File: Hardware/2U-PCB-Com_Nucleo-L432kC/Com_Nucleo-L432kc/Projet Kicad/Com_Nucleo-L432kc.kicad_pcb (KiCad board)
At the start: 2 copper layers, 90 x 92 mm, 46 parts, among them IC1 PCI_EXPRESS_CARD, J1 Bus Standard, J2 I2C_Grove, J3 I2C_Grove, J4 Conn_01x08, J5 Conn_01x08, J6 Conn_01x15, J7 Conn_01x15, J8 I2C_Grove, J9 I2C_Grove, SW101 Jumper_RESET_L432KC_Open, SW102 Jumper_MCU_Reset_Open, SW103 Jumper_SX1303_Reset_Open, U1 7404

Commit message: routage terminé
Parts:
- removed B1, B2: SN74AHC1G125DBVT, Package_SO:TSOP-5_1.65x3.05mm_P0.95mm
- removed C11: 100n, Capacitor_SMD:C_0805_2012Metric_Pad1.18x1.45mm_HandSolder
- removed the C7 at (135.9, 60.6)
- removed the C8 at (132.9, 60.6)
- removed the J2 at (79.0, 51.0)
- removed the J4 at (70.9, 79.6)
- removed R4, R5: 100, Resistor_SMD:R_0805_2012Metric_Pad1.20x1.40mm_HandSolder
- removed REF** (x2): MountingHole_2.7mm_M2.5_Pad, MountingHole:MountingHole_2.7mm_M2.5_Pad
- removed SW102: Jumper_MCU_Reset_Open, Button_Switch_THT:SW_PUSH_6mm
- removed SW103: Jumper_SX1303_Reset_Open, Button_Switch_THT:SW_PUSH_6mm
- removed U1: 7404, Library:N14
- added JP1: PWM1_SEL, Connector_PinHeader_1.27mm:PinHeader_1x03_P1.27mm_Vertical, F.Cu at (132.8, 122.8)
- added JP3: RX_SEL, Connector_PinHeader_1.27mm:PinHeader_1x03_P1.27mm_Vertical, F.Cu at (149.4, 125.4)
- added JP5: INT_SEL, Connector_PinHeader_1.27mm:PinHeader_1x03_P1.27mm_Vertical, F.Cu at (139.3, 125.4)
- added R10: 0, Resistor_SMD:R_0805_2012Metric_Pad1.20x1.40mm_HandSolder, F.Cu at (90.2, 61.9)
- added R11: 0, Resistor_SMD:R_0805_2012Metric_Pad1.20x1.40mm_HandSolder, F.Cu at (92.2, 61.8)
- added R12: 0, Resistor_SMD:R_0805_2012Metric_Pad1.20x1.40mm_HandSolder, F.Cu at (87.3, 61.8)
- added R13: 0, Resistor_SMD:R_0805_2012Metric_Pad1.20x1.40mm_HandSolder, F.Cu at (85.3, 61.8)
- added R14: 0, Resistor_SMD:R_0805_2012Metric_Pad1.20x1.40mm_HandSolder, F.Cu at (82.4, 61.8)
- added R15: 0, Resistor_SMD:R_0805_2012Metric_Pad1.20x1.40mm_HandSolder, F.Cu at (80.4, 61.8)
- added R8: 0, Resistor_SMD:R_0805_2012Metric_Pad1.20x1.40mm_HandSolder, F.Cu at (107.1, 97.8)
- added R9: 0, Resistor_SMD:R_0805_2012Metric_Pad1.20x1.40mm_HandSolder, F.Cu at (107.1, 94.6)
- added U2: MCP9808_MSOP, Package_SO:MSOP-8_3x3mm_P0.65mm, F.Cu at (77.0, 56.6)
- CR1: footprint Library:SO-8_STM -> Package_SO:SO-8_3.9x4.9mm_P1.27mm
- G*** (x2): footprint Com Nucleo library:logo_csug -> Com_L432KC_footprint:logo_csug
- J1: footprint Library:flatsat_conn -> Com_L432KC_footprint:flatsat_conn
- J5: value Conn_01x08 -> MIKROE-4247; footprint Library:MIkrobus_Connector -> Com_L432KC_footprint:MIKROE4247
- JP4: value Jumper_STANDBY_GPS_Open -> TX_SEL; footprint Connector_PinHeader_2.54mm:PinHeader_1x02_P2.54mm_Vertical -> Connector_PinHeader_1.27mm:PinHeader_1x03_P1.27mm_Vertical
- R1, R2: value 0 -> 4K7
- R3: value 100 -> 4K7
- R6: value 100 -> 0
- R7: moved to F.Cu
- SW1: renamed from SW101; value Jumper_RESET_L432KC_Open -> Reset
- moved R2 82.8 mm to (94.8, 52.2), turned to -90 degrees
- moved R1 59.6 mm to (141.3, 59.6)
- moved J6 55.8 mm to (71.1, 113.4)
- moved J4 55.8 mm to (93.9, 113.4)
- moved J9 55.8 mm to (82.1, 113.4)
- moved R3 50.3 mm to (98.5, 52.2), turned to -90 degrees
- moved R6 33.6 mm to (132.1, 88.7), turned to 180 degrees
- moved R7 32.6 mm to (132.6, 63.3), turned to 180 degrees
- moved JP2 24.8 mm to (118.8, 77.9), turned to 180 degrees
- moved G*** 21.7 mm to (103.6, 109.9)
- moved JP4 21.0 mm to (145.3, 125.4), turned to 180 degrees
- moved J5 8.88 mm to (93.8, 88.5), turned to 90 degrees
- moved SW1 8.65 mm to (140.3, 56.5)
- moved G*** 3.15 mm to (85.0, 54.5)
- moved C9 2.85 mm to (115.0, 93.5)
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- renumbered C6 to C10, C13 to C2, C2 to C3, C14 to C4, C3 to C5, C4 to C6, C9 to C7, C5 to C8, C10 to C9, J7 to J2, J3 to J4, J8 to J6, J6 to J7, JP5 to JP2
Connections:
- net /CAN1_RX renamed /CAN_RX
- net /CAN1_TX renamed /CAN_TX
- net /MCU_MOSI renamed /INT1
- C7 pad 1: +3V3 -> Net-(CR1-VS)
- C9 pad 1: +3V3 -> Net-(CR1-VS)
- CR1 pad 3: +3V3 -> Net-(CR1-VS)
- IC1 pad 13: Net-(IC1-REFCLK+) -> unconnected-(IC1-REFCLK+-Pad13)
- IC1 pad 19: unconnected-(IC1-RESERVED-Pad19) -> /PPS_LORA_CORE
- IC1 pad 22: /SX1303_RESET -> /RST_LORA_CORE
- IC1 pad 23: Net-(IC1-PERn0) -> unconnected-(IC1-PERn0-Pad23)
- IC1 pad 25: /STANDBY_GPS -> unconnected-(IC1-PERp0-Pad25)
- IC1 pad 30: /SCL -> unconnected-(IC1-SMB_SCL-Pad30)
- IC1 pad 31: unconnected-(IC1-PETn0-Pad31) -> /UART_TX_LORA_CORE
- IC1 pad 32: /SDA -> unconnected-(IC1-SMB_SDA-Pad32)
- IC1 pad 33: unconnected-(IC1-PETp0-Pad33) -> /UART_RX_LORA_CORE
- IC1 pad 45: Net-(IC1-RESERVED1) -> /SCLK
- IC1 pad 47: Net-(IC1-RESERVED2) -> /MISO
- IC1 pad 49: Net-(IC1-RESERVED3) -> /MOSI
- IC1 pad 51: Net-(IC1-RESERVED4) -> /CS_LORA_CORE
- IC1 pad 6: /TH1 -> /GPIO6_SX1303
- J1 pad 11: /SENS_MAG-Y -> /SENS2
- J1 pad 17: /RX_CALC -> /UART_RX_INISAT
- J1 pad 19: /TX_CALC -> /UART_TX_INISAT
- J1 pad 3: /Vin -> +5V
- J1 pad 30: /RESET_SIGNAL -> unconnected-(J1-PWM_O_1-Pad30)
- J1 pad 4: unconnected-(J1-5V-Pad4) -> +5V
- J1 pad 6: /PWM_ROUE/MAG-X -> /PWM_INISAT
- J1 pad 8: /SENS_ROUE/MAG-X -> /SENS1
- J1 pad 9: /PWM_MAG-Y -> /PWM2
- J2 pad 10: unconnected-(J7-Pin_10-Pad10) -> Net-(J2-Pin_10)
- J2 pad 11: unconnected-(J7-Pin_11-Pad11) -> Net-(J2-Pin_11)
- J2 pad 12: /PWM_ROUE/MAG-X -> /PWM1
- J2 pad 14: /MCU_NRESET -> /MOSI
- J2 pad 15: /CS_MCU -> /MISO
- J2 pad 3: /L432KC_RESET -> /RESET_GENERAL
- J2 pad 6: /PWM_MAG-Y -> /RST_LORA_CORE
- J2 pad 7: /RX_CALC -> /UART_RX_1
- J2 pad 8: /TX_CALC -> /UART_TX_1
- J2 pad 9: /PWM_MKR -> /CS_LORA_CORE
- J5 pad 1: /PWM_MKR -> GND
- J5 pad 2: /INT_MKR -> +5V
- J5 pad 3: unconnected-(J5-Pin_3-Pad3) -> /SDA
- J5 pad 4: unconnected-(J5-Pin_4-Pad4) -> /SCL
- J5 pad 5: /SCL -> /UART_TX_MK
- J5 pad 6: /SDA -> /UART_RX_MK
- J5 pad 7: unconnected-(J5-Pin_7-Pad7) -> /INT_MK
- J5 pad 8: GND -> /PWM_MK
- J7 pad 1: /Vin -> Net-(J7-Pin_1)
- J7 pad 10: /GPIO(6) -> /UART_RX_INISAT
- J7 pad 11: /HOST_SCK -> /SENS1
- J7 pad 12: /SENS_ROUE/MAG-X -> /SENS2
- J7 pad 14: /3.3V -> Net-(J7-Pin_14)
- J7 pad 15: /SENS_MAG-Y -> /SCLK
- J7 pad 3: unconnected-(J6-Pin_3-Pad3) -> Net-(J7-Pin_3)
- J7 pad 4: Net-(J6-Pin_4) -> Net-(J7-Pin_4)
- J7 pad 5: /INT_MKR -> /UART_TX_INISAT
- J7 pad 7: /MISO -> /PWM2
- J7 pad 8: /RESET_SIGNAL -> /CS_MK
- J7 pad 9: /AN -> /GPIO6_SX1303
- JP4 pad 1: /STANDBY_GPS -> /UART_RX_LORA_CORE
- JP4 pad 2: GND -> /UART_TX_1
- L432KC1 pad 10: unconnected-(L432KC1-D7-Pad10) -> Net-(J2-Pin_10)
- L432KC1 pad 11: unconnected-(L432KC1-D8-Pad11) -> Net-(J2-Pin_11)
- L432KC1 pad 12: /PWM_ROUE/MAG-X -> /PWM1
- L432KC1 pad 14: /MCU_NRESET -> /MOSI
- L432KC1 pad 15: /CS_MCU -> /MISO
- L432KC1 pad 16: /SENS_MAG-Y -> /SCLK
- L432KC1 pad 17: /3.3V -> Net-(J7-Pin_14)
- L432KC1 pad 19: /SENS_ROUE/MAG-X -> /SENS2
- L432KC1 pad 20: /HOST_SCK -> /SENS1
- L432KC1 pad 21: /GPIO(6) -> /UART_RX_INISAT
- L432KC1 pad 22: /AN -> /GPIO6_SX1303
- L432KC1 pad 23: /RESET_SIGNAL -> /CS_MK
- L432KC1 pad 24: /MISO -> /PWM2
- L432KC1 pad 26: /INT_MKR -> /UART_TX_INISAT
- L432KC1 pad 27: Net-(J6-Pin_4) -> Net-(J7-Pin_4)
- L432KC1 pad 28: unconnected-(L432KC1-RESET-Pad28) -> Net-(J7-Pin_3)
- L432KC1 pad 3: /L432KC_RESET -> /RESET_GENERAL
- L432KC1 pad 30: /Vin -> Net-(J7-Pin_1)
- L432KC1 pad 6: /PWM_MAG-Y -> /RST_LORA_CORE
- L432KC1 pad 7: /RX_CALC -> /UART_RX_1
- L432KC1 pad 8: /TX_CALC -> /UART_TX_1
- L432KC1 pad 9: /PWM_MKR -> /CS_LORA_CORE
- R1 pad 1: /MCU_NRESET -> +3V3
- R1 pad 2: Net-(IC1-REFCLK+) -> /RESET_GENERAL
- R2 pad 1: /MCU_NRESET -> +3V3
- R2 pad 2: Net-(IC1-PERn0) -> /SCL
- R3 pad 1: /HOST_SCK -> +3V3
- R3 pad 2: Net-(IC1-RESERVED1) -> /SDA
- R6 pad 1: /CS_MCU -> +3V3
- R6 pad 2: Net-(IC1-RESERVED4) -> Net-(J7-Pin_14)
- R7 pad 1: /TH1 -> +5V
- R7 pad 2: /GPIO(6) -> Net-(J7-Pin_4)
- SW1 pad 1: /L432KC_RESET -> /RESET_GENERAL
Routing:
- net /MCU_NRESET: track 230.0 -> 0.00 mm, vias 3 -> 0
- net /CS_MCU: track 137.6 -> 0.00 mm, vias 3 -> 0
- net /HOST_SCK: track 135.0 -> 0.00 mm, vias 1 -> 0
- net /SX1303_RESET: track 124.3 -> 0.00 mm
- net /UART_TX_MK: track 0.00 -> 104.7 mm
- net /UART_RX_1: track 0.00 -> 104.0 mm
- net /UART_RX_MK: track 0.00 -> 103.9 mm
- net /INT_MK: track 0.00 -> 101.3 mm
- net /PWM_MK: track 0.00 -> 99.2 mm
- net /UART_TX_1: track 0.00 -> 98.7 mm, vias 0 -> 1
- net Net-(B2-OE): track 97.5 -> 0.00 mm, vias 1 -> 0
- net /SCLK: track 0.00 -> 96.7 mm
- net /RESET_GENERAL: track 0.00 -> 84.7 mm
- net /TH1: track 81.7 -> 0.00 mm, vias 1 -> 0
- net +5V: track 0.00 -> 77.5 mm, vias 0 -> 2
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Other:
- board text added: "RX"
- board text added: "TX"
- board text added: "UART"
- board text removed: "x"

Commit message: ajout documentation
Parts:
- added R4: 4K7, Resistor_SMD:R_0805_2012Metric_Pad1.20x1.40mm_HandSolder, F.Cu at (138.5, 61.8)
- J2, J7: footprint Connector_PinSocket_2.54mm:PinSocket_1x15_P2.54mm_Vertical -> Connector_PinHeader_2.54mm:PinHeader_1x15_P2.54mm_Vertical
- moved G*** 25.5 mm to (82.2, 79.9)
- moved JP2 22.6 mm to (134.4, 61.5)
- moved C2 2.74 mm to (77.0, 86.1)
- moved C4 2.74 mm to (77.0, 88.7)
- moved JP1 2.53 mm to (132.8, 125.4), turned to 180 degrees
- moved G*** 1.96 mm to (104.0, 108.0)
- moved R7 1.15 mm to (133.0, 64.3)
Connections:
- JP2 pad 2: +3V3 -> GND
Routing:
- net Net-(CR1-ASC): track 8.74 -> 48.3 mm
- net +3V3: track 402.1 -> 372.1 mm
- net /RESET_GENERAL: track 84.7 -> 89.2 mm
- net /PWM_INISAT: track 63.7 -> 68.1 mm
- net /PWM_MK: track 99.2 -> 100.3 mm
- net Net-(J7-Pin_4): track 7.82 -> 8.73 mm
- net +5V: track 77.5 -> 76.9 mm
- net GND: vias 60 -> 74
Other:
- board text added: "A0"
- board text added: "A1"
- board text added: "A2"
- board text added: "CAN high speed"
- board text added: "MK"
- board text added: "Main Reset"
- board text added: "PCI"
- board text added: "Persyval Lab LSI Carnot"
- board text removed: "Persyval Lab - LSI Carnot"

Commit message: ajout documentation bis
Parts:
- JP1, JP3, JP4, JP5: footprint Connector_PinHeader_1.27mm:PinHeader_1x03_P1.27mm_Vertical -> Connector_PinHeader_2.54mm:PinHeader_1x03_P2.54mm_Vertical
- moved JP4 1.23 mm to (145.2, 126.6)
- moved JP5 1.23 mm to (139.3, 126.6)
- moved JP1 1.23 mm to (132.8, 126.6)
- moved JP3 1.23 mm to (149.4, 126.6)
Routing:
- net /UART_RX_LORA_CORE: track 40.3 -> 43.8 mm
- net /INT_MK: track 101.3 -> 104.6 mm
- net /UART_RX_MK: track 103.9 -> 107.2 mm
- net /UART_TX_MK: track 104.7 -> 107.8 mm
- net /PPS_LORA_CORE: track 26.4 -> 28.3 mm
- net /UART_TX_LORA_CORE: track 42.5 -> 44.4 mm
- net /UART_RX_1: track 104.0 -> 105.8 mm
- net /PWM_INISAT: track 68.1 -> 68.8 mm
- net /PWM_MK: track 100.3 -> 100.8 mm
- net GND: vias 74 -> 75

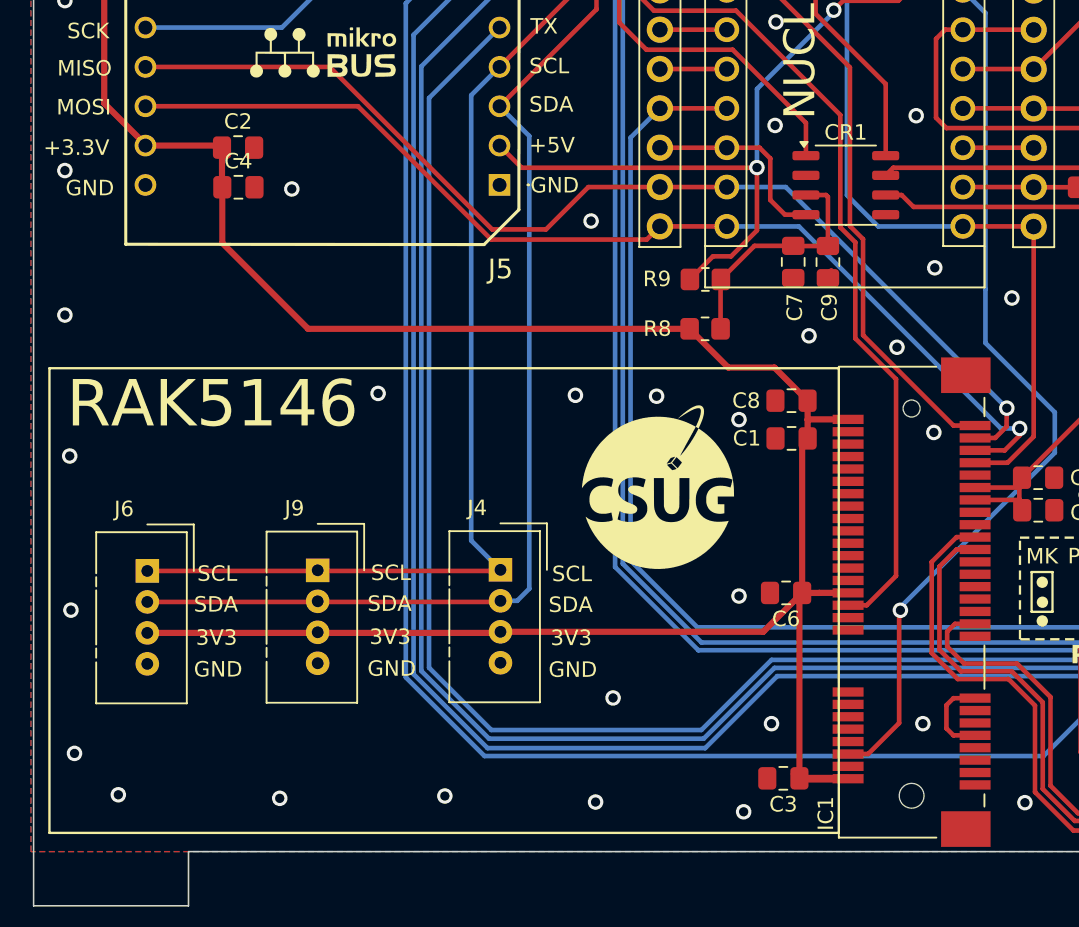
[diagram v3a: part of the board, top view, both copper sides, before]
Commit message: ajout trous entretoise pour support mini PCI Express
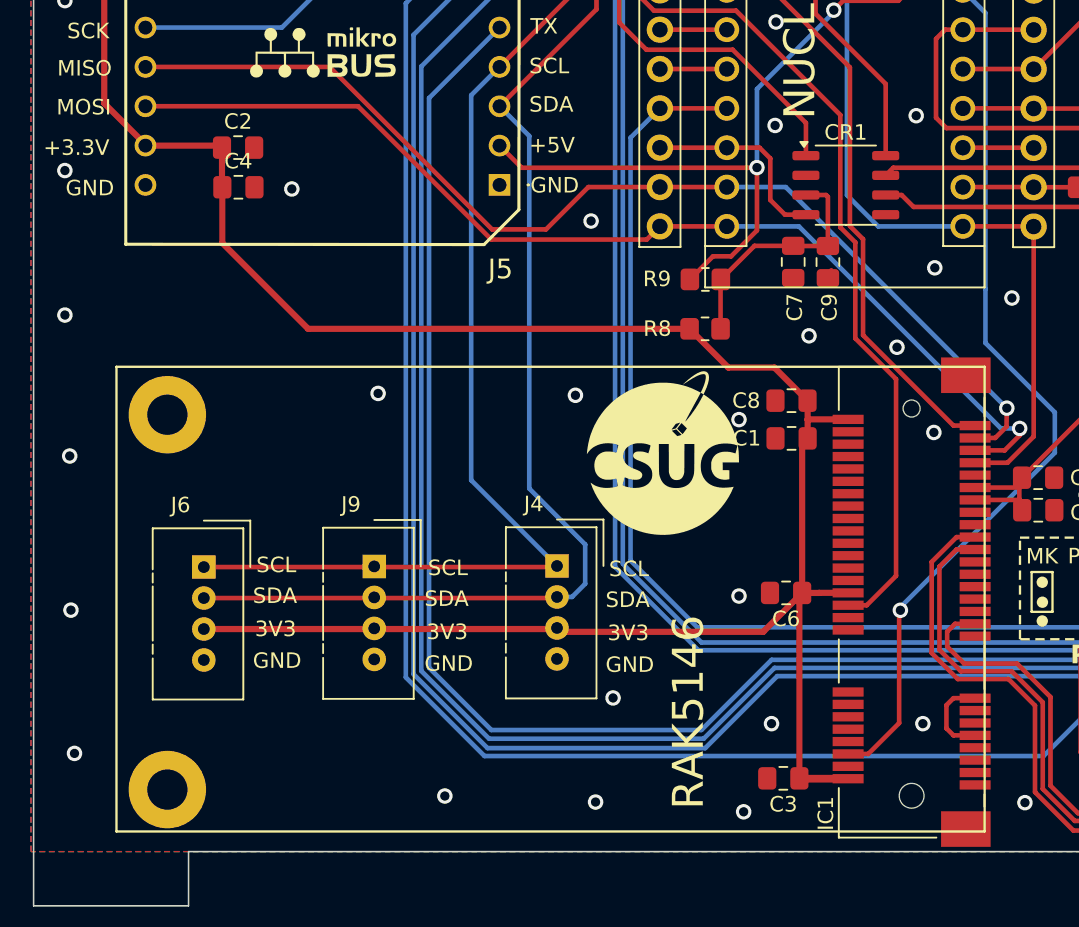
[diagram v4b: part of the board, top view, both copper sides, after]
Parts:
- added ?: , , F.Cu at (72.4, 103.3)
- added REF**: support mini PCI, Com_L432KC_footprint:support mini PCI, F.Cu at (72.4, 127.5)
- moved J4 3.66 mm to (97.5, 113.1)
- moved J6 3.66 mm to (74.7, 113.2)
- moved J9 3.66 mm to (85.7, 113.1)
- moved G*** 2.22 mm to (104.3, 105.8)
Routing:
- net +3V3: track 372.1 -> 368.5 mm
- net /SCL: track 202.6 -> 203.8 mm
- net /SDA: track 217.6 -> 218.7 mm
- net GND: vias 75 -> 73

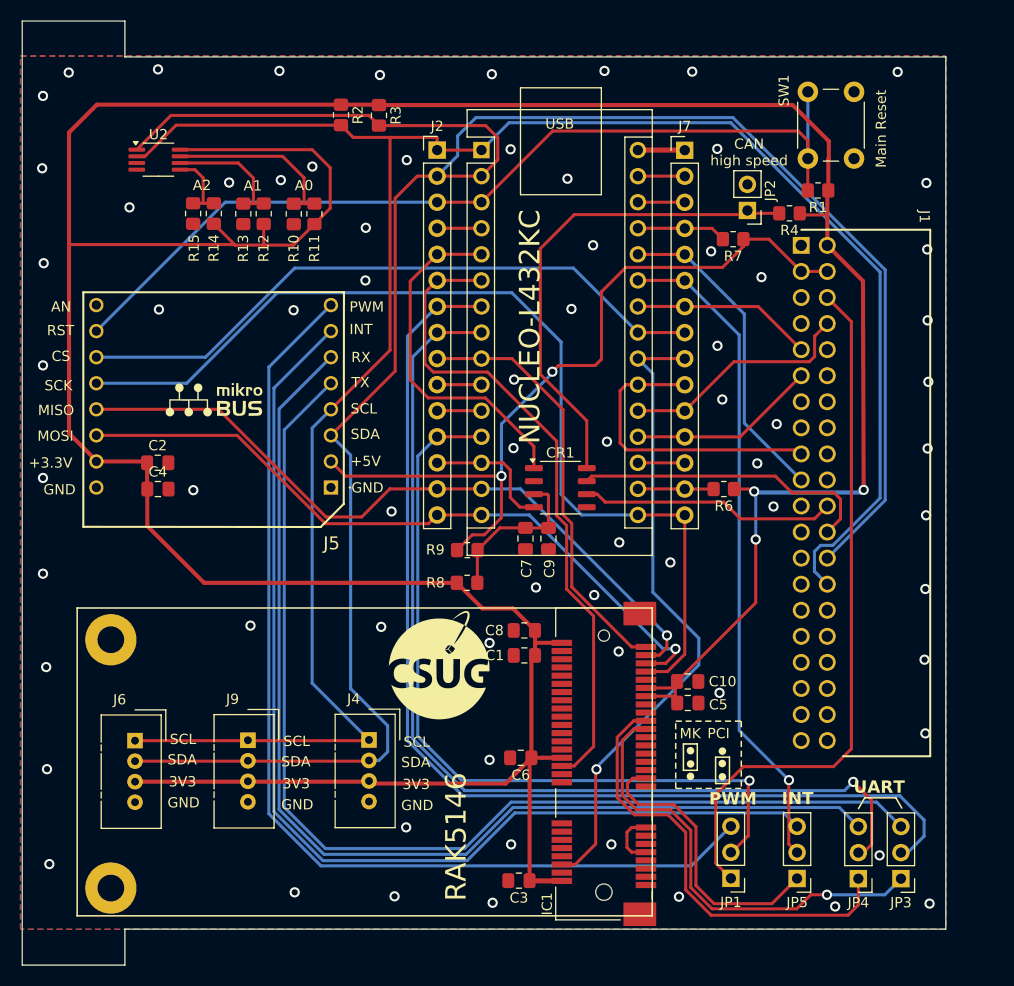
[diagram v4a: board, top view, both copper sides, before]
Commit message: fix mauvaise empreinte connecteur
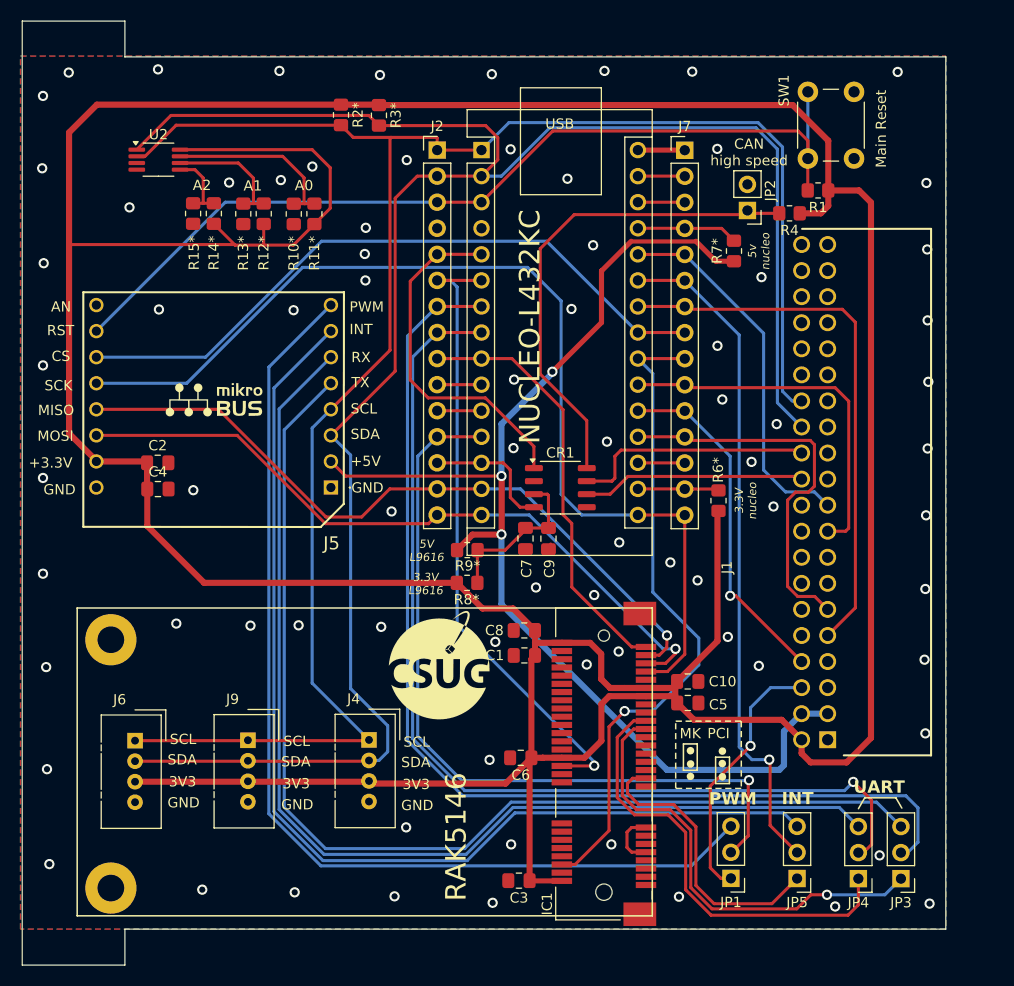
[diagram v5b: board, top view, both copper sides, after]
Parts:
- moved J1 11.0 mm to (141.5, 89.0)
- moved R6* 1.24 mm to (131.6, 89.8), turned to 90 degrees
- moved R7* 1.15 mm to (133.1, 65.5), turned to 90 degrees
- renumbered R10 to R10*, R11 to R11*, R12 to R12*, R13 to R13*, R14 to R14*, R15 to R15*, R2 to R2*, R3 to R3*, R6 to R6*, R7 to R7*, R8 to R8*, R9 to R9*
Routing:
- net +3V3: track 368.5 -> 426.1 mm, vias 3 -> 0
- net /PWM_INISAT: track 68.8 -> 25.5 mm, vias 0 -> 1
- net +5V: track 76.9 -> 116.4 mm, vias 2 -> 3
- net /PWM2: track 17.7 -> 53.5 mm
- net /SDA: track 218.7 -> 194.7 mm
- net /SCL: track 203.8 -> 181.1 mm
- net /SENS2: track 18.4 -> 38.0 mm
- net /SENS1: track 23.1 -> 34.2 mm, vias 0 -> 1
- net /CAN_TD: track 29.6 -> 23.6 mm
- net /UART_RX_INISAT: track 29.7 -> 35.8 mm
- net /UART_TX_INISAT: track 31.3 -> 36.4 mm
- net /SCLK: track 96.7 -> 101.1 mm
- net GND: track 15.2 -> 10.9 mm, vias 73 -> 78
- net /CAN_RD: track 25.0 -> 21.8 mm
- net /CS_MK: track 63.6 -> 65.7 mm
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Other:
- board text added: "3.3V L9616"
- board text added: "3.3V nucleo"
- board text added: "5V L9616"
- board text added: "5v nucleo"

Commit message: finalisation Thingsat Inisat v1.0
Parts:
- moved G*** 55.1 mm to (70.4, 62.3)
- renumbered R10* to R10, R11* to R11, R12* to R12, R13* to R13, R14* to R14, R15* to R15, R2* to R2, R3* to R3, R6* to R6, R7* to R7, R8* to R8, R9* to R9
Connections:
- J5 pad 13: /MOSI -> /MISO
- J5 pad 14: /MISO -> /MOSI
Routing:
- net /MOSI: track 70.6 -> 69.6 mm, vias 1 -> 2
- net /MISO: track 69.6 -> 70.7 mm
